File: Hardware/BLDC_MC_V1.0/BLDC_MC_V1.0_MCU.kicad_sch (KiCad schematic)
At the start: 41 parts, among them J3 USB_C_Receptacle_USB2.0_16P, J4 Conn_02x03_Counter_Clockwise, SW1 SW_Push, U4 STM32G431RBTx, U9 USBLC6-2SC6, Y1 7M-24.000MAAJ-T, Y2 ABS07-32.768KHZ-T

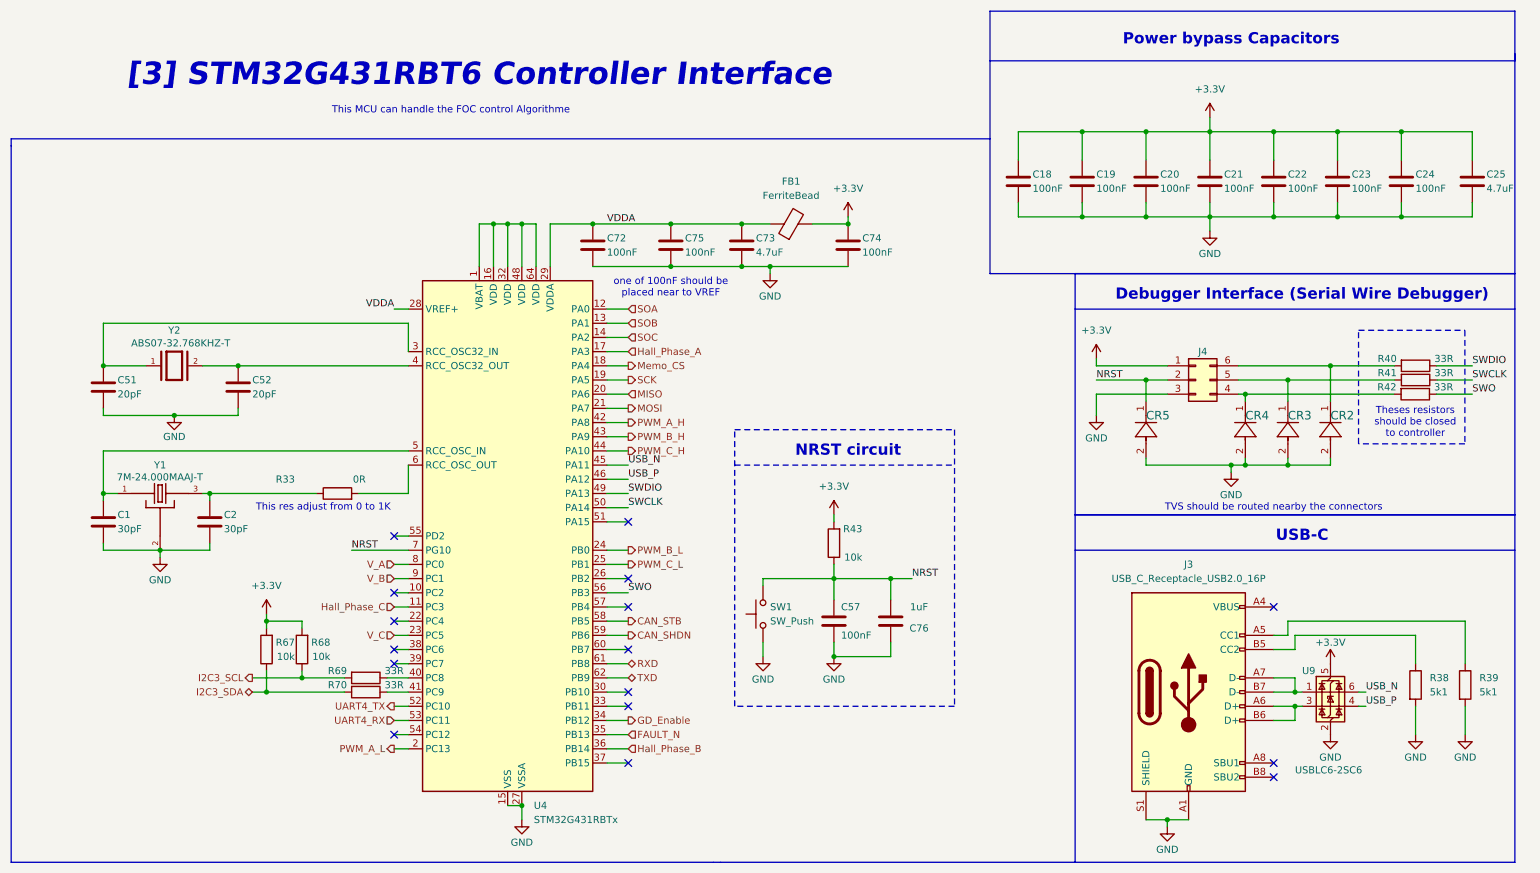
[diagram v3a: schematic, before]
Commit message: Add in series resistors for PWM pins and Test points for the same pins
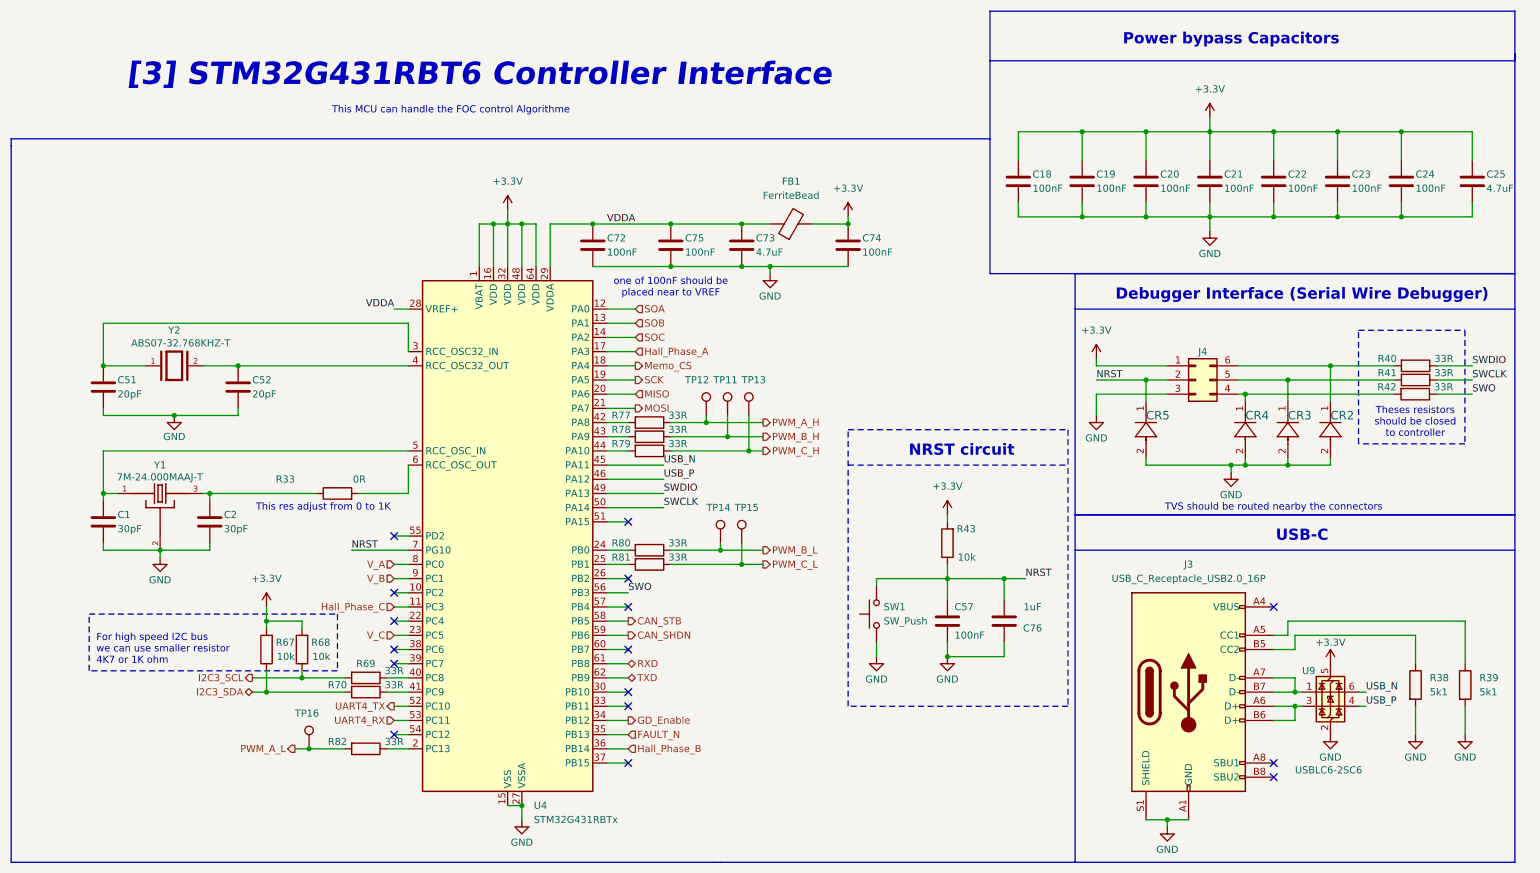
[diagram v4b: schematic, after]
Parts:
- added R77, R78, R79, R80, R81, R82: 33R, Resistor_SMD:R_0603_1608Metric, symbol Device:R
- added TP11, TP12, TP13, TP14, TP15, TP16: TestPoint, Connector_Pin:Pin_D0.9mm_L10.0mm_W2.4mm_FlatFork, symbol Connector:TestPoint
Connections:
- net +3.3V: now also U4.1 (VBAT), U4.16 (VDD), U4.32 (VDD), U4.48 (VDD), U4.64 (VDD)
- net PWM_A_H: now also R77.1, TP12.1; no longer U4.42 (PA8)
- net PWM_A_L: now also R82.2, TP16.1; no longer U4.2 (PC13)
- net PWM_B_H: now also R78.1, TP11.1; no longer U4.43 (PA9)
- net PWM_B_L: now also R80.1, TP14.1; no longer U4.24 (PB0)
- net PWM_C_H: now also R79.1, TP13.1; no longer U4.44 (PA10)
- net PWM_C_L: now also R81.1, TP15.1; no longer U4.25 (PB1)
- new net: R82.1, U4.2 (PC13)
- new net: R80.2, U4.24 (PB0)
- new net: R81.2, U4.25 (PB1)
- new net: R77.2, U4.42 (PA8)
- new net: R78.2, U4.43 (PA9)
- new net: R79.2, U4.44 (PA10)
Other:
- note added: "For high speed I2C bus we can use smaller resistor 4K7 or 1K ohm"
- moved on the sheet: C57, C76, R43, SW1

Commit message: Solve all errors and wornings in project
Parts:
- removed U4: STM32G431RBTx, Package_QFP:LQFP-64_10x10mm_P0.5mm, symbol MCU_ST_STM32G4:STM32G431RBTx
- added U4: STM32G431RBT6, BLDC_Motor_Driver_Components_Footprint:LQFP64-10x10mm, symbol STM32G431RBT6:STM32G431RBT6
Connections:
- net +3.3V: now also U4.1 (VBAT), U4.16 (VDD1), U4.32 (VDD2), U4.48 (VDD3), U4.64 (VDD4)
- net CAN_SHDN: now also U4.59 (PB6)
- net CAN_STB: now also U4.58 (PB5)
- net FAULT_N: now also U4.35 (PB13)
- net GD_Enable: now also U4.34 (PB12)
- net GND: now also U4.15 (VSS1), U4.27 (VSSA), U4.31 (VSS2), U4.47 (VSS3), U4.63 (VSS4)
- net Hall_Phase_A: now also U4.17 (PA3)
- net Hall_Phase_B: now also U4.36 (PB14)
- net Hall_Phase_C: now also U4.11 (PC3)
- net MISO: now also U4.20 (PA6)
- net MOSI: now also U4.21 (PA7)
- net Memo_CS: now also U4.18 (PA4)
- net NRST: now also U4.7 (PG10)
- net RXD: now also U4.61 (PB8)
- net SCK: now also U4.19 (PA5)
- net SOA: now also U4.12 (PA0)
- net SOB: now also U4.13 (PA1)
- net SOC: now also U4.14 (PA2)
- net SWCLK: now also U4.50 (PA14)
- net SWDIO: now also U4.49 (PA13)
- net SWO: now also U4.56 (PB3)
- net TXD: now also U4.62 (PB9)
- net UART4_RX: now also U4.53 (PC11)
- net UART4_TX: now also U4.52 (PC10)
- net USB_N: now also U4.45 (PA11)
- net USB_P: now also U4.46 (PA12)
- net V_A: now also U4.8 (PC0)
- net V_B: now also U4.9 (PC1)
- net V_C: now also U4.23 (PC5)
- net at R82.1: now also U4.2 (PC13)
- net at R80.2: now also U4.24 (PB0)
- net at R81.2: now also U4.25 (PB1)
- net at C51.1, Y2.1: now also U4.3 (PC14)
- net at C52.1, Y2.2: now also U4.4 (PC15)
- net at R69.1: now also U4.40 (PC8)
- net at R70.1: now also U4.41 (PC9)
- net at R77.2: now also U4.42 (PA8)
- net at R78.2: now also U4.43 (PA9)
- net at R79.2: now also U4.44 (PA10)
- net at C1.1, Y1.1: now also U4.5 (PF0)
- net at R33.2: now also U4.6 (PF1)
- net VDDA renamed Vref
- net Vref: now also U4.28 (VREF+), U4.29 (VDDA)
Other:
- title: (none) -> ${Project_Name}

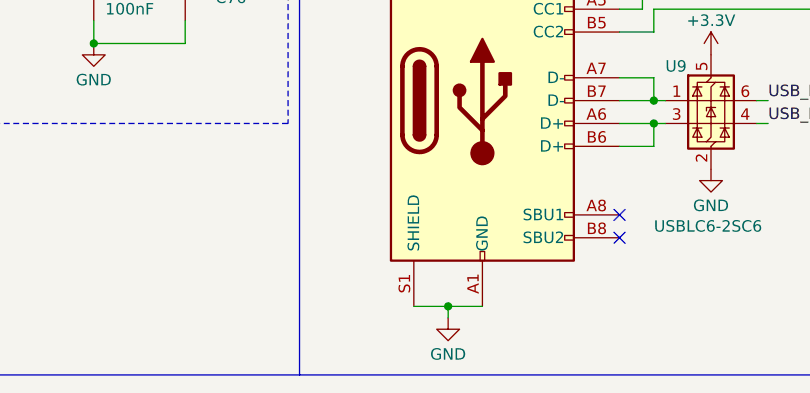
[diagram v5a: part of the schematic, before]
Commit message: Run DRC and solve all errors and warnings (project updated to Kicad 10)
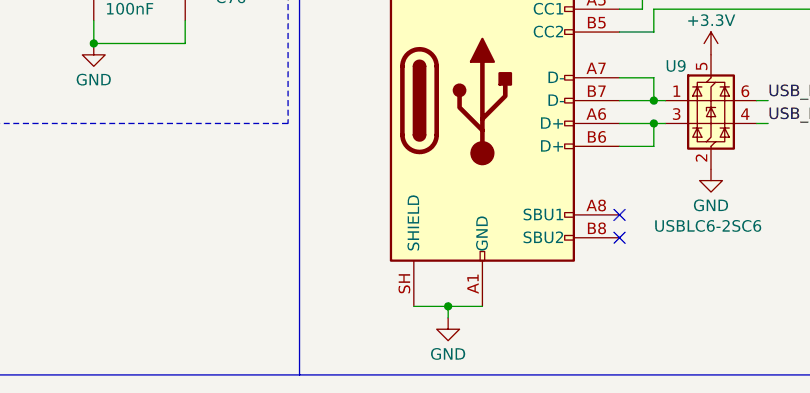
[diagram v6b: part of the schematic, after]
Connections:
- net GND: now also J3.SH (SHIELD); no longer J3.S1 (SHIELD)

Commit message: Update recovery files of the project
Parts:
- removed TP11, TP12, TP13, TP14, TP15, TP16: TestPoint, Connector_Pin:Pin_D0.9mm_L10.0mm_W2.4mm_FlatFork, symbol Connector:TestPoint
